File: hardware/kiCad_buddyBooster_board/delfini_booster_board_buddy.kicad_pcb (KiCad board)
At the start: 2 copper layers, 150 parts, among them J1 Screw_Terminal_1x04, J2 Screw_Terminal_1x04, J3 Screw_Terminal_1x04, J4 Screw_Terminal_1x04, J5 1792229, J6 1792229, J7 Screw_Terminal_1x04, J8 1792229, J9 1792229, P1 CONN_01X03, P10 CONN_01X03, P11 CONN_01X03, P12 CONN_01X03, P13 CONN_01X03, P14 CONN_01X02, P15 CONN_01X03, P16 CONN_01X02, P17 CONN_01X02, P18 CONN_01X03, P19 CONN_01X03, P2 CONN_01X05, P20 CONN_01X03, P21 CONN_01X03, P22 CONN_01X01, P23 CONN_01X01, P24 CONN_01X01, P25 CONN_01X03, P26 CONN_01X01, P27 CONN_01X01, P28 CONN_01X01, P29 CONN_01X03, P3 CONN_01X05, P30 CONN_01X03, P31 CONN_01X03, P32 CONN_01X01, P33 CONN_01X04, P34 CONN_01X04, P4 CONN_02X10, P5 CONN_02X10, P6 CONN_02X10, P7 CONN_02X10, P8 CONN_01X03, P9 CONN_01X03, Q1 2N7002, Q2 2N7002, Q3 2N7002, Q4 2N7002, Q5 IRF9540N, Q6 IRF9540N, Q7 2N7002, U1 TMP275, U2 T90-Relay, U3 tps2112a, U4 LM7812, U5 R-783.3-1.0, U6 T90-Relay, U7 TXB0104

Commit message: - Placement of parts - Need relay protection for mosfet. and freewheel diode for load.
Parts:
- U7: footprint digikey-footprints:TSSOP-16-1EP_W4.40mm -> digikey-footprints:TSSOP-14_W4.4mm
- moved P25 256.5 mm to (135.3, 182.7), turned to 90 degrees
- moved R30 239.8 mm to (215.9, 139.7)
- moved P10 234.1 mm to (64.2, 148.4)
- moved C13 231.8 mm to (150.6, 151.0)
- moved P17 231.1 mm to (175.3, 156.2)
- moved C20 226.4 mm to (179.1, 157.5)
- moved R32 226.3 mm to (228.6, 154.9)
- moved C10 221.9 mm to (228.6, 142.2)
- moved C19 220.2 mm to (179.1, 158.8)
- moved F2 218.5 mm to (193.0, 142.2)
- moved L2 217.7 mm to (177.8, 161.3)
- moved R31 216.4 mm to (166.4, 158.8)
- moved Q3 216.1 mm to (226.1, 148.6)
- moved U3 216.0 mm to (163.8, 152.4)
- moved R39 215.8 mm to (203.2, 139.7)
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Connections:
- J2 pad 1: +12V -> GND
- J2 pad 2: /TO_ENCODER_L_A -> /TO_ENCODER_L_B
- J2 pad 3: /TO_ENCODER_L_B -> /TO_ENCODER_L_A
- J2 pad 4: GND -> +12V
- J4 pad 1: +12V -> GND
- J4 pad 2: /TO_ENCODER_R_A -> /TO_ENCODER_R_B
- J4 pad 3: /TO_ENCODER_R_B -> /TO_ENCODER_R_A
- J4 pad 4: GND -> +12V

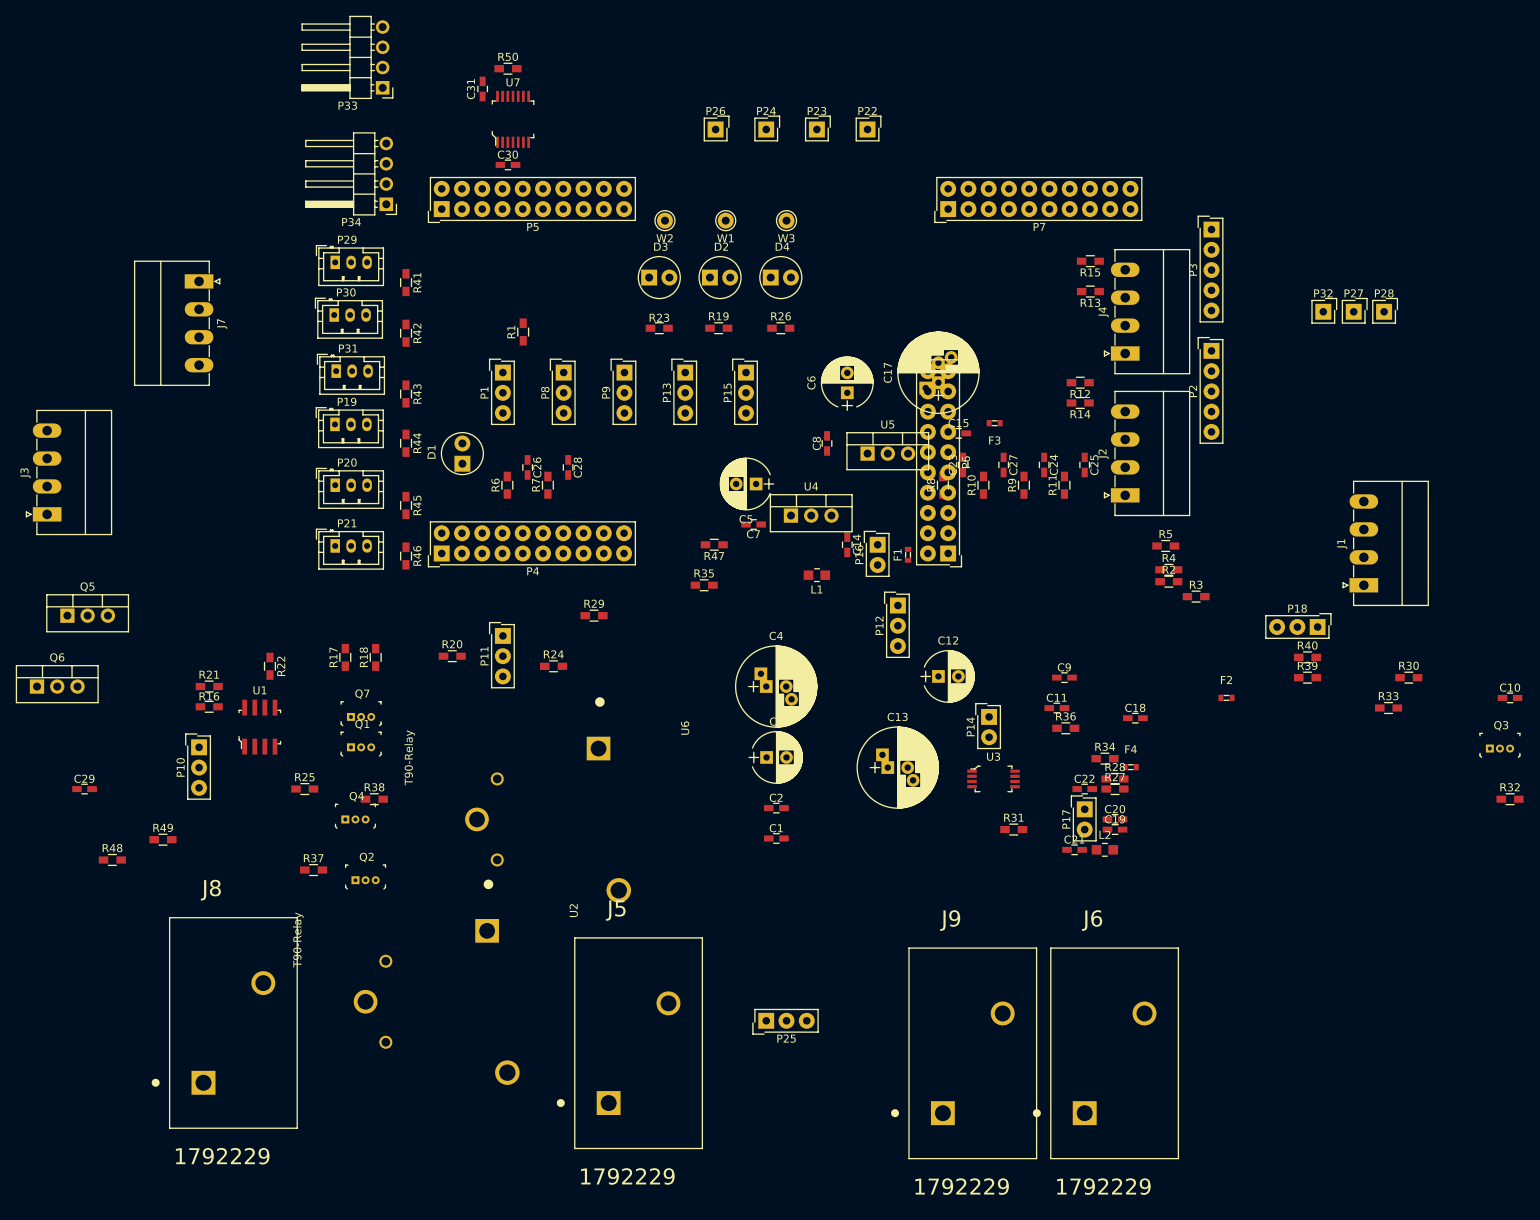
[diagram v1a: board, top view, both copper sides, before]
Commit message: - Placement grouped - added I2C - moved a few pins around. need FW sync with hw - connected UART to Sabertooth
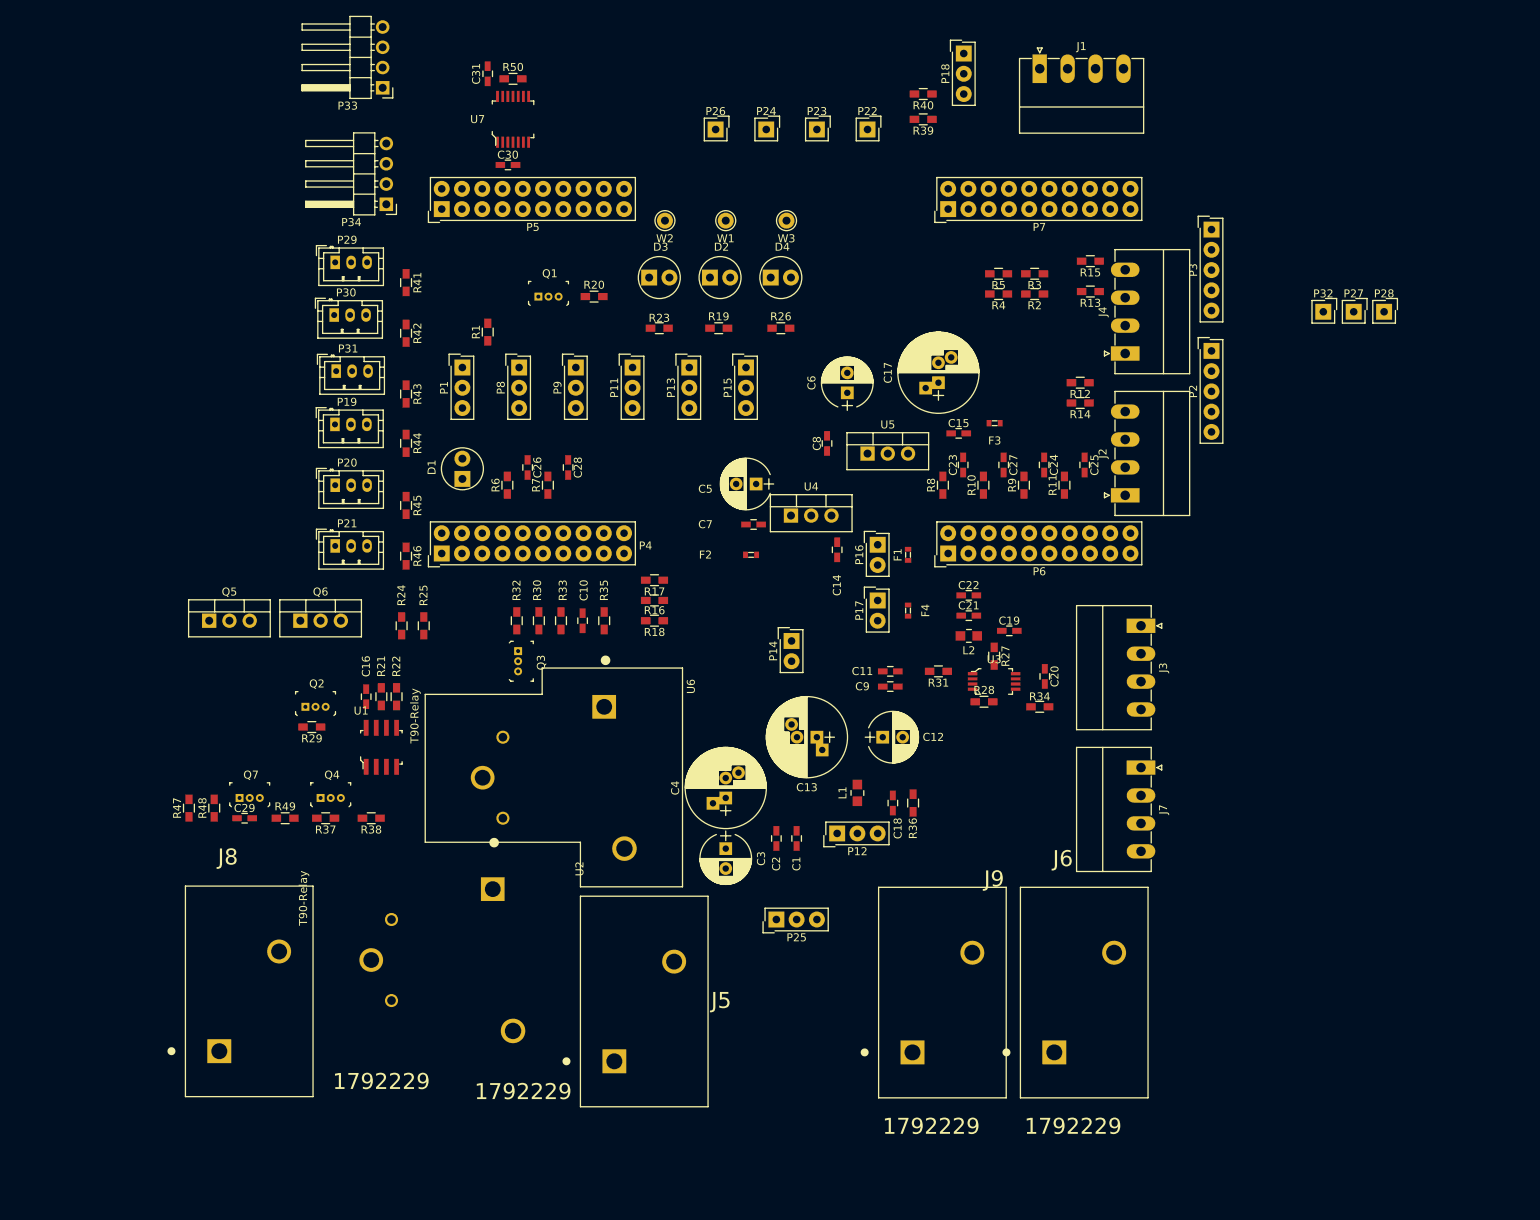
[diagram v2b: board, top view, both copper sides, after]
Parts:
- removed P10: CONN_01X03, Connectors_Samtec:SL-103-X-XX_1x03
- added C16: C_Small, Capacitors_SMD:C_0603_HandSoldering, F.Cu at (85.2, 142.1)
- moved J3 137.9 mm to (182.3, 133.2), turned to 270 degrees
- moved J7 132.9 mm to (182.3, 151.0)
- moved R32 126.5 mm to (104.0, 132.6), turned to 90 degrees
- moved Q3 122.5 mm to (104.2, 136.4), turned to 270 degrees
- moved C10 116.7 mm to (112.3, 132.6), turned to 90 degrees
- moved R30 109.3 mm to (106.8, 132.6), turned to 90 degrees
- moved R33 104.3 mm to (109.6, 132.6), turned to 90 degrees
- moved R40 85.5 mm to (155.0, 66.5), turned to 180 degrees
- moved R39 85.0 mm to (155.0, 69.7), turned to 180 degrees
- moved P18 84.5 mm to (160.1, 61.4), turned to 0 degrees
- moved J1 76.5 mm to (169.6, 63.3), turned to 0 degrees
- moved R47 73.7 mm to (62.9, 156.1), turned to 90 degrees
- moved F2 62.3 mm to (133.4, 124.3), turned to 180 degrees
- moved Q1 61.2 mm to (106.8, 91.9)
- moved R16 57.4 mm to (121.3, 130.0), turned to 180 degrees
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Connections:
- P12 pad 1: Net-(L1-Pad1) -> /BAT_PWR_IN
- P12 pad 2: /BAT_PWR_IN -> Net-(L1-Pad1)
- P4 pad 15: Net-(P4-Pad15) -> /TMP275_ALERT_OD
- P4 pad 17: Net-(P4-Pad17) -> /SDA_4.7K
- P4 pad 19: Net-(P4-Pad19) -> /SCL_4.7K
- P4 pad 5: Net-(P4-Pad5) -> /TEST_EN_N
- P6 pad 13: Net-(P6-Pad13) -> /UART_SABER_TX
- P6 pad 15: /TEST_EN_N -> Net-(P6-Pad15)
- R21 pad 1: Net-(P10-Pad2) -> +3V3
- U1 pad 8: Net-(P10-Pad2) -> +3V3

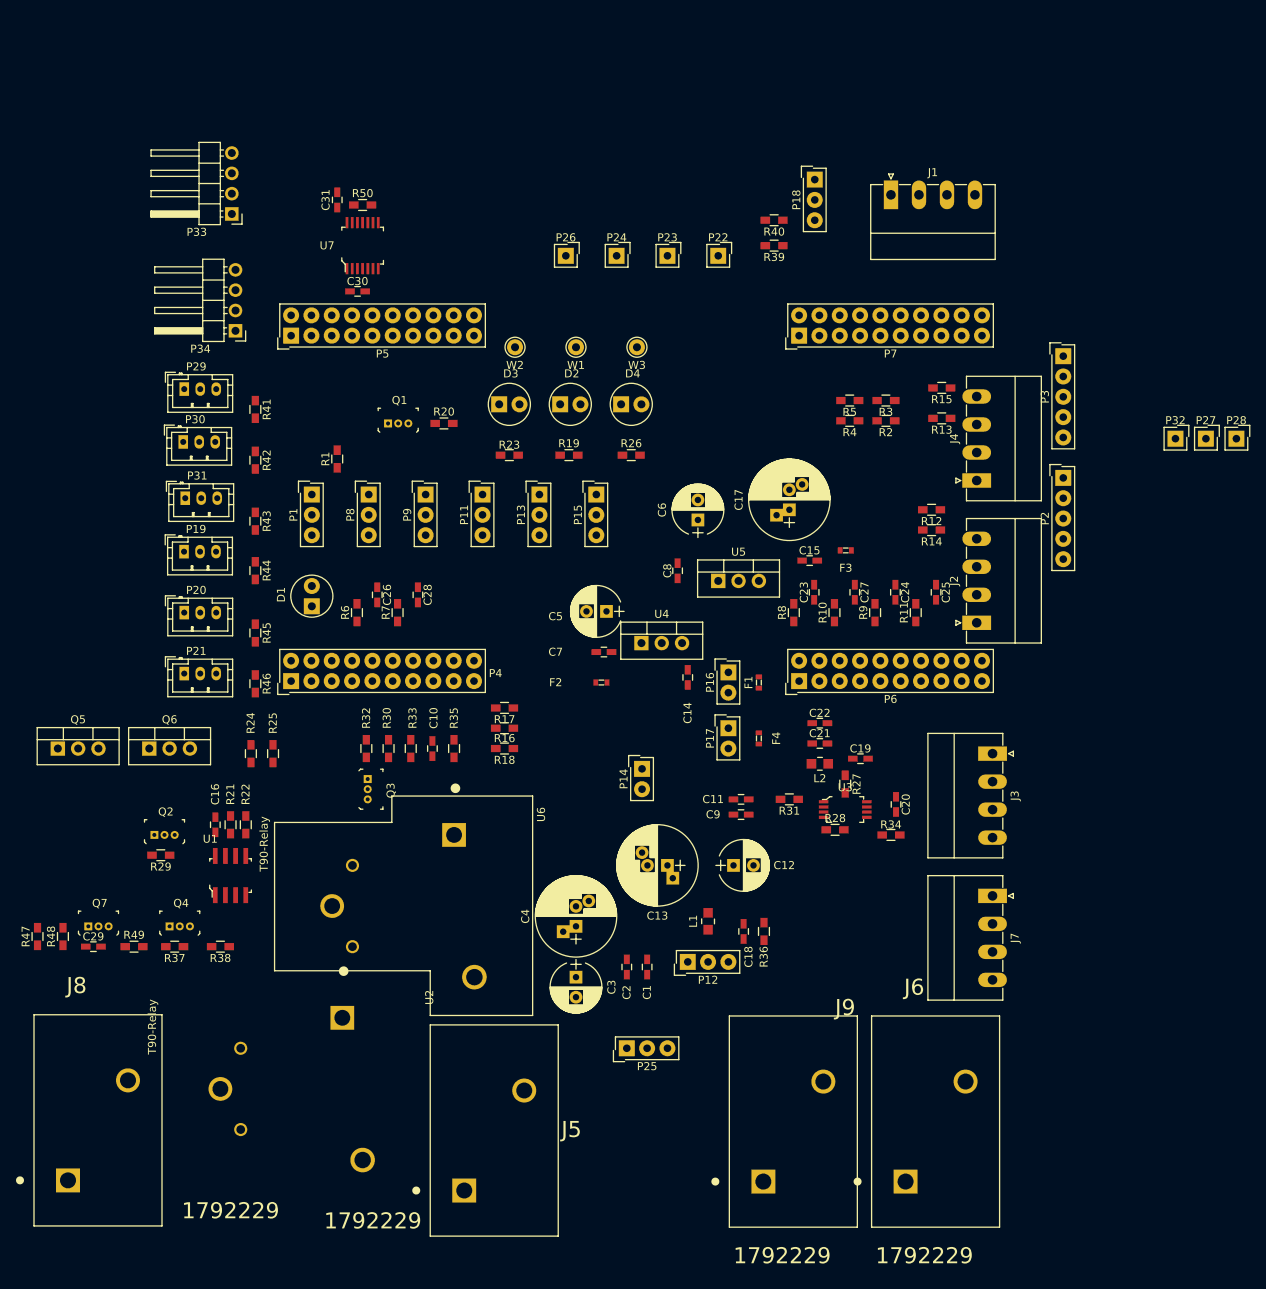
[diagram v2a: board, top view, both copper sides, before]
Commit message: - Continue to massage the parts - Changed regulators 3v3 and 12V to have correct pin number
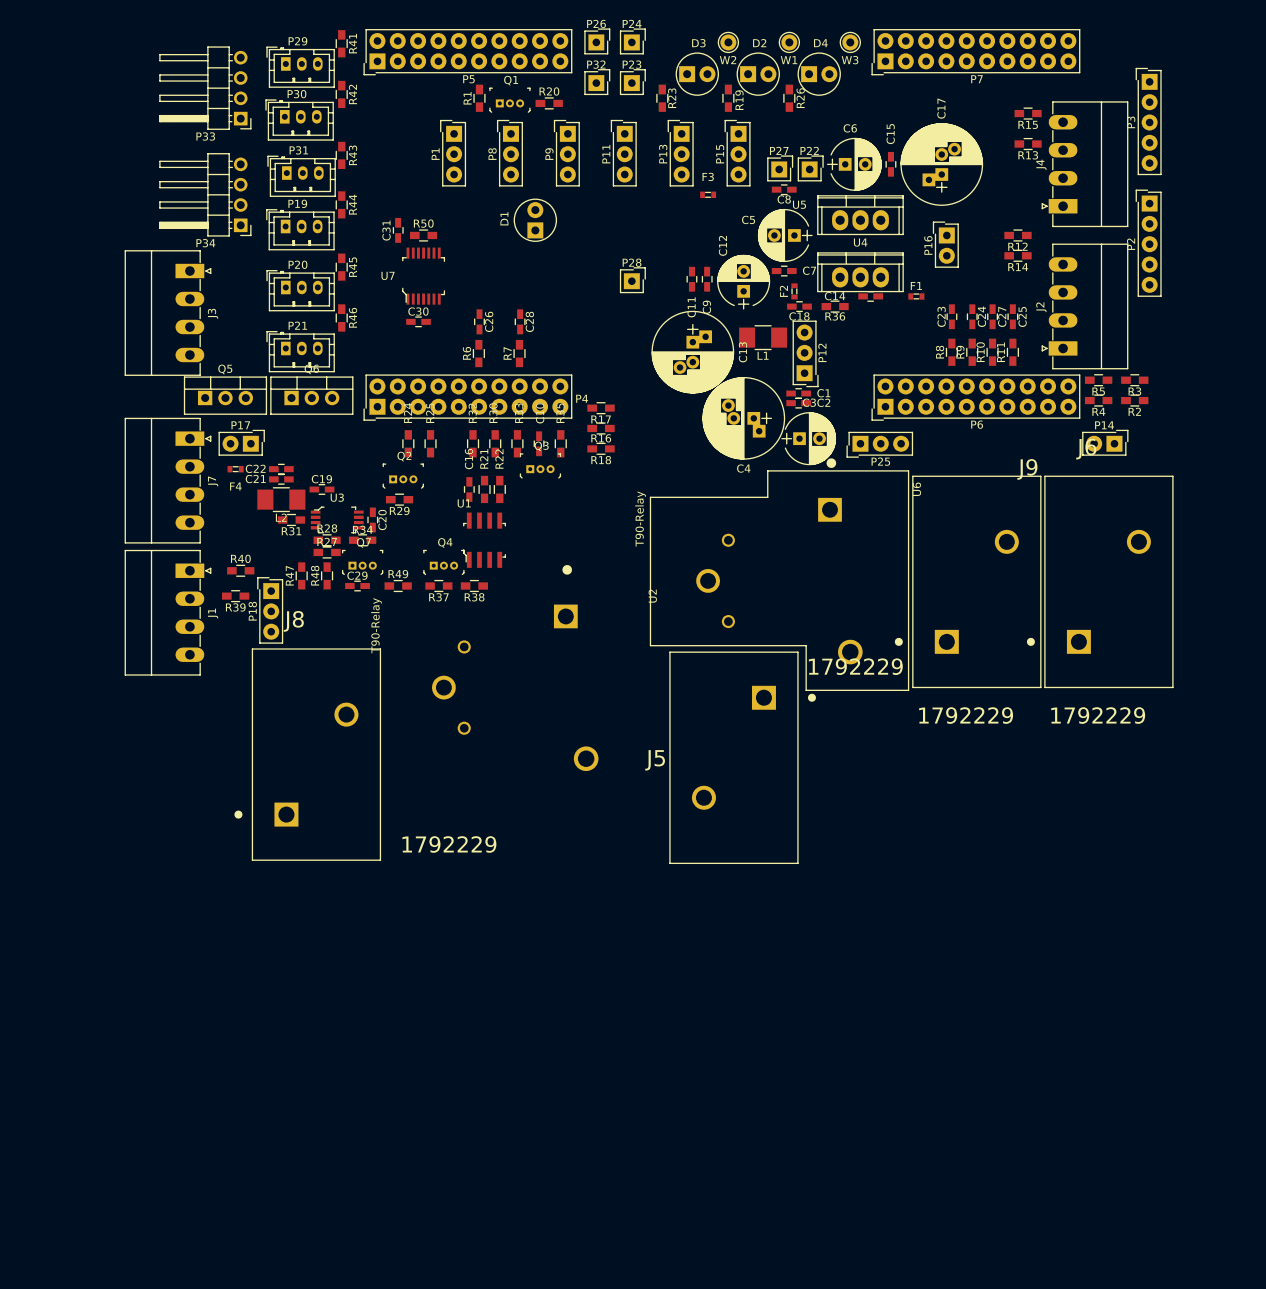
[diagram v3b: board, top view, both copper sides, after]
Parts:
- L1, L2: footprint digikey-footprints:0805 -> Resistors_SMD:R_1210_HandSoldering
- U4, U5: footprint TO_SOT_Packages_THT:TO-220-3_Vertical -> TO-220
- moved J3 117.1 mm to (82.0, 72.9)
- moved J7 115.5 mm to (82.0, 93.8)
- moved J1 99.4 mm to (82.0, 110.3), turned to 270 degrees
- moved P18 85.2 mm to (92.2, 112.9)
- moved P32 84.9 mm to (132.8, 49.4)
- moved P25 81.0 mm to (165.8, 94.5)
- moved R39 80.3 mm to (87.7, 113.5)
- moved R40 79.8 mm to (88.3, 110.3), turned to 0 degrees
- moved R36 78.6 mm to (162.6, 77.3), turned to 180 degrees
- moved C18 78.4 mm to (158.2, 77.3), turned to 0 degrees
- moved P28 78.1 mm to (137.2, 74.1)
- moved R34 75.6 mm to (103.6, 106.5)
- moved C19 75.3 mm to (98.5, 100.2)
- moved P12 75.0 mm to (158.8, 85.6), turned to 180 degrees
- moved C21 75.0 mm to (93.4, 98.9)
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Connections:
- U4 pad 1: (no net) -> VAA
- U4 pad 2: (no net) -> GND
- U4 pad 3: (no net) -> Net-(C14-Pad1)
- U5 pad 1: (no net) -> VAA
- U5 pad 2: (no net) -> GND
- U5 pad 3: (no net) -> Net-(C15-Pad1)

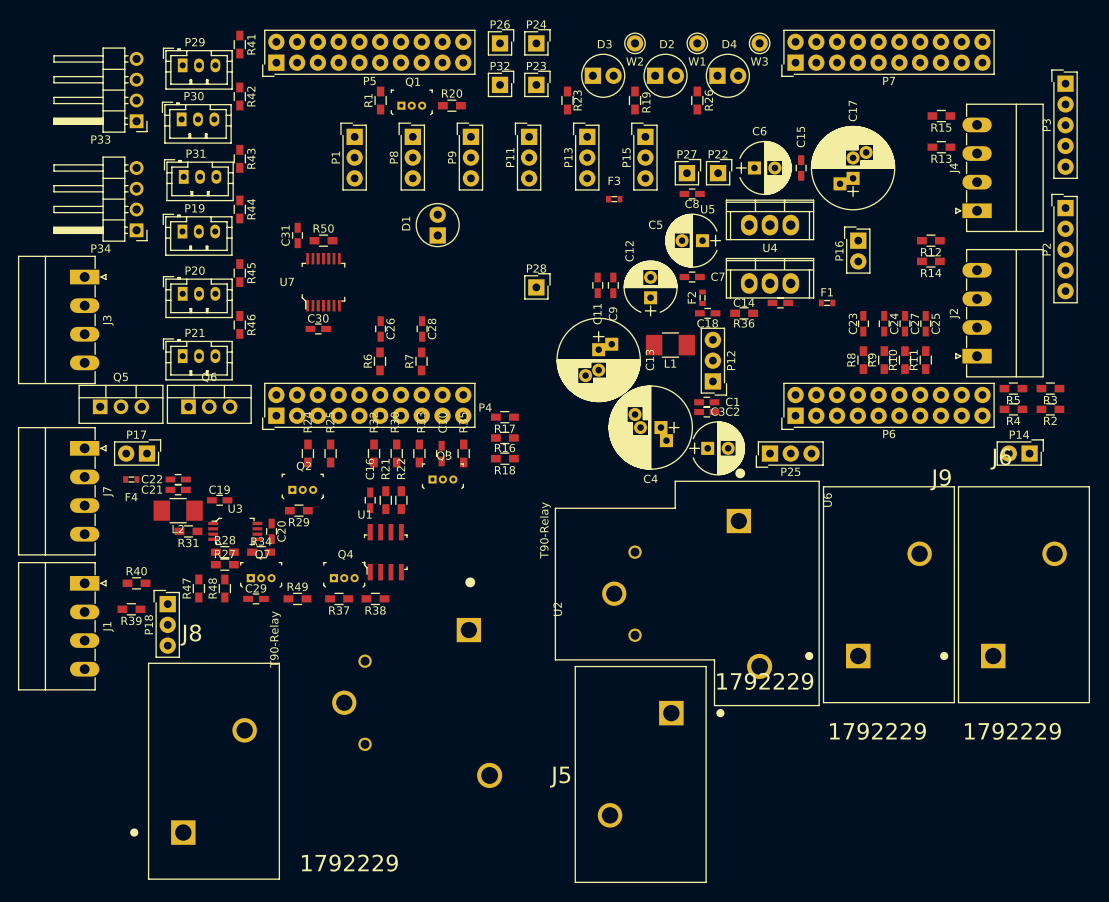
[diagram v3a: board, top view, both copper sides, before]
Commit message: -PCB- updated relay top silk -PCB- drawn outline in Tsilk
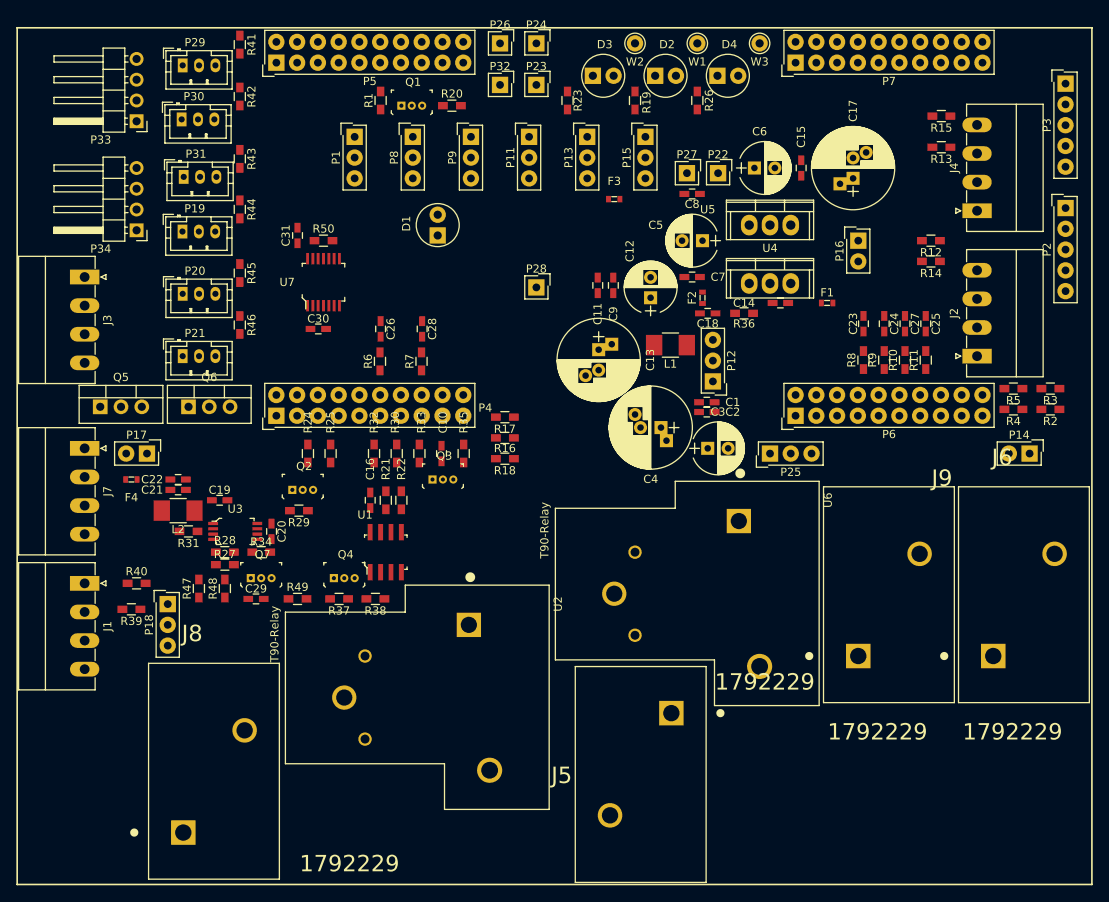
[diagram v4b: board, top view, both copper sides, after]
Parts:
- moved U2 0.64 mm to (122.6, 124.3)
